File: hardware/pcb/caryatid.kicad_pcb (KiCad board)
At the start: 2 copper layers, 150 x 90 mm, 131 parts, among them J1 DC in, J10 FSR, J11 Digital bus, J12 RGB status, J13 Comms A - Qwiic, J14 Mic bias return, J15 Comms B - module, J16 Expansion / SPI1, J17 Audio out L/R/G, J18 Audio in L/R/rtn, J19 Comms A - module, J3 Latch switch, J4 Charge LEDs, J5 Analogue bus, J6 SW1 switch, J7 SW2 switch, J8 SW3 switch, J9 Soft pot, U1 BQ24074RGT, U2 TPS61023DRL, U3 74HC14, U4 MCP6002

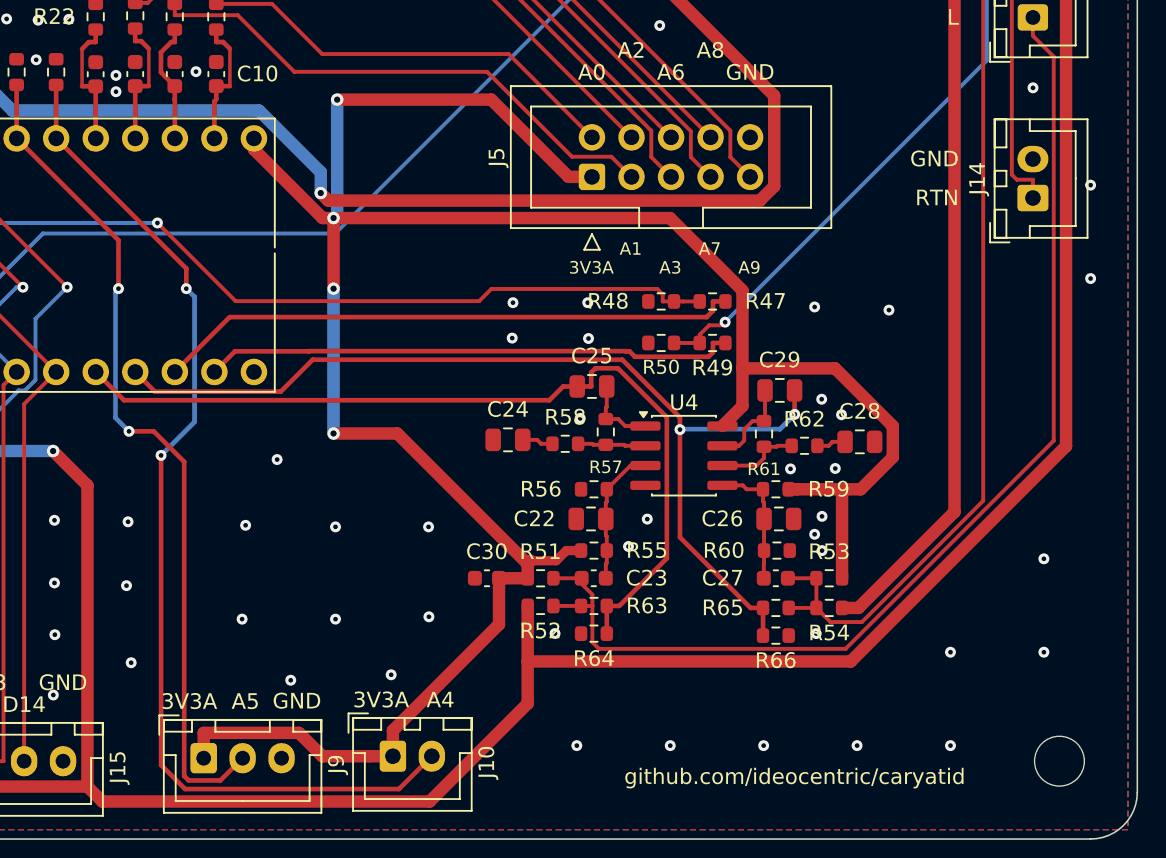
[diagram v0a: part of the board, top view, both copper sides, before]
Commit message: Source JP1-3: C52016391, verified against live JLC data
HX PH254-01-03-Z-L11.5, 1x3P 2.54mm through-hole header, 3A, gold
plated brass. 56393 in stock, MOQ 2, $0.0249 at 1-199, Extended,
manualWeld so JLC hand-solders it.

The L11.5 model number resolves to a 2.5 mm body with 6 mm of mating
pin, which is the length a standard 2.54 mm shunt needs, and puts the
top of a fitted shunt about 8.5 mm above the board -- far below the
26.91 mm stack, so it costs no headroom.

THE SHUNTS ARE NOT A PLACED COMPONENT. JLC will not fit a jumper cap;
it is an accessory, not a part on the board. Buying separately, noted
in lcsc.yaml so nobody looks for it on the BOM later.

Gate now reports 107 of 110 covered. The three still open are R51 2k2,
R52 220R and R67 392R -- and the first two were never a gap that got
missed: they were DNP, so they never reached a BOM export, and the
sourcing sweep only ever saw parts that do. Populating the front-end is
what surfaced them.

Recorded for the search: every 0603 resistor on this board is UNI-ROYAL
0603WAF series, all twelve of them, so the three outstanding values have
predictable manufacturer part numbers -- 0603WAF2201T5E, 0603WAF2200T5E
and 0603WAF3920T5E. The E24 values on this board are all Basic and the
E96 values all Extended, so R67 should be expected to carry a loading
fee and the other two not.
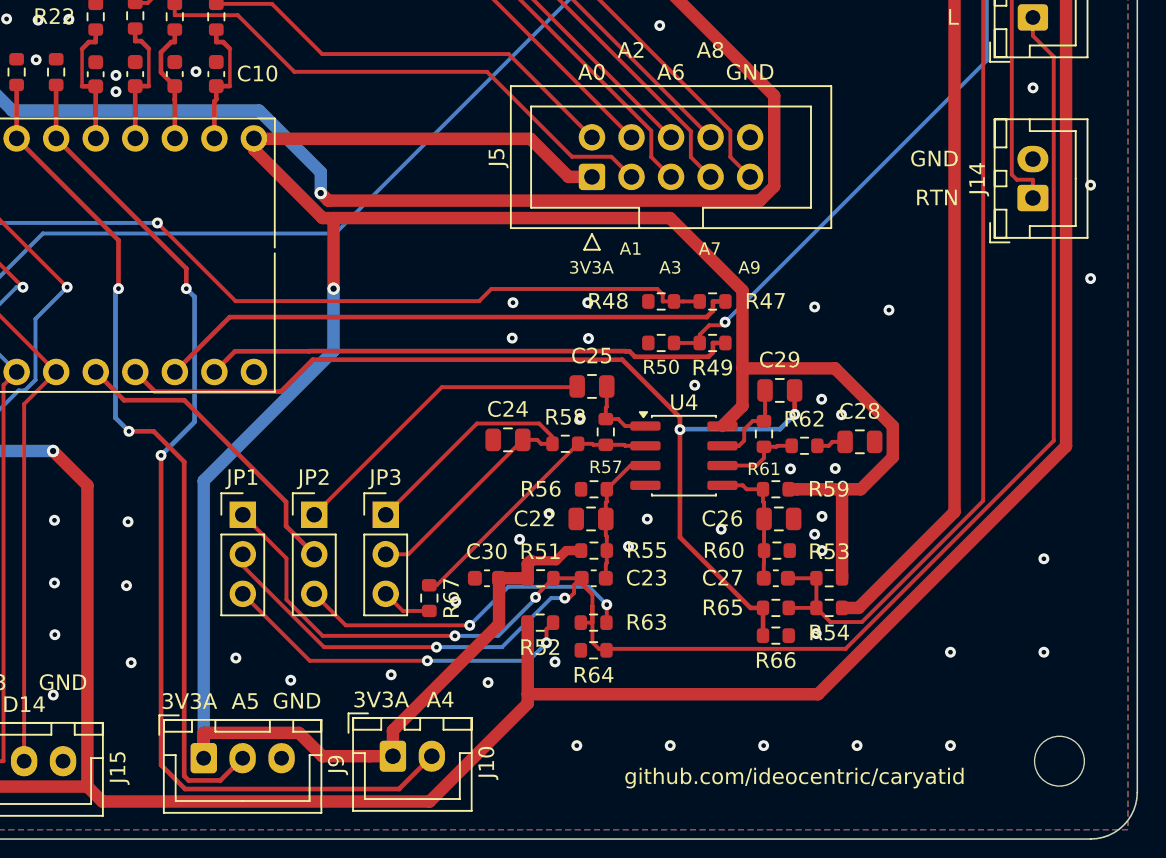
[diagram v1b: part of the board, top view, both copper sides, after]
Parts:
- added JP1: Mic bias select, Connector_PinHeader_2.54mm:PinHeader_1x03_P2.54mm_Vertical, F.Cu at (142.5, 99.2)
- added JP2: Mic path select, Connector_PinHeader_2.54mm:PinHeader_1x03_P2.54mm_Vertical, F.Cu at (147.1, 99.2)
- added JP3: Mic gain select, Connector_PinHeader_2.54mm:PinHeader_1x03_P2.54mm_Vertical, F.Cu at (151.7, 99.2)
- added R67: 392R, Resistor_SMD:R_0603_1608Metric, F.Cu at (154.5, 104.5)
- moved R52 1.07 mm to (161.7, 106.1)
- moved R63 1.07 mm to (165.1, 106.1)
- moved R64 1.07 mm to (165.1, 107.9)
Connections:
- C25 pad 2: AUDIO_IN_L -> AMP_OUT_L
- R51 pad 2: /audio/MIC_L -> /audio/BIAS_E_L
- R52 pad 2: /audio/MIC_L -> /audio/BIAS_C_L
- R58 pad 2: /audio/GAINLEG_L -> /audio/LEG_101_L
- R63 pad 2: AUDIO_IN_L -> BYPASS_L
- R64 pad 1: AUDIO_IN_L -> BYPASS_L
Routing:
- net AUDIO_IN_L: track 56.1 -> 19.8 mm
- net /audio/MIC_L: track 71.8 -> 97.9 mm, vias 0 -> 2
- net /audio/BIAS_E_L: track 0.00 -> 25.9 mm, vias 0 -> 2
- net /audio/BIAS_C_L: track 0.00 -> 23.2 mm, vias 0 -> 2
- net BYPASS_L: track 0.00 -> 22.3 mm, vias 0 -> 2
- net AMP_OUT_L: track 0.00 -> 20.3 mm
- net /audio/LEG_101_L: track 0.00 -> 13.5 mm
- net /audio/OPA_L_N: track 4.37 -> 17.7 mm
- net /audio/GAINLEG_L: track 2.01 -> 13.9 mm
- net +3V3A: track 162.6 -> 167.6 mm, vias 4 -> 1
- net /audio/LEG_256_L: track 0.00 -> 3.26 mm

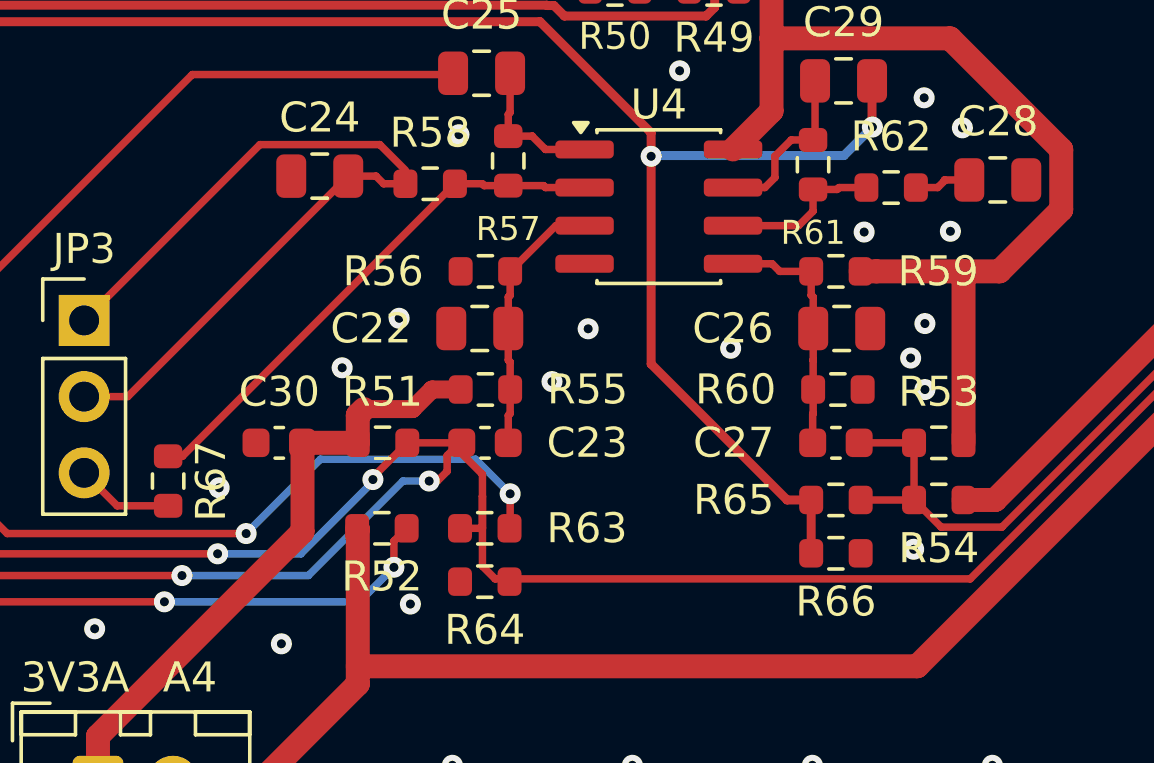
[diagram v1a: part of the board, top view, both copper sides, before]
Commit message: Delete four stale tracks the net split left shorting, and tidy up
Rewiring the mic front-end moved four pads onto new nets. KiCad reassigns
PAD nets on update but leaves existing TRACKS alone, so the tracks that
used to serve those pads stayed put and now touched pads of a different
net -- four real shorts that would have arrived as dead boards.

  GAINLEG_L  0.73 mm  shorting R58.2 LEG_101_L
  MIC_L      1.82 mm  shorting R51.2 BIAS_E_L
  MIC_L      0.60 mm  shorting R64.1 BYPASS_L
  MIC_L     15.84 mm  shorting R64.1 BYPASS_L

Matched on net AND both endpoints so no similar segment elsewhere could
be hit, and all four had to match or nothing was written.

A scan I wrote first reported 32 candidates and was wrong -- it treated
any track passing near a pad as overlapping, ignoring clearance. DRC is
the authority here and it says four. Recording that because the crude
version looked authoritative and would have sent someone chasing
twenty-eight phantoms.

Also: R67 reference moved from local -1.43 to -1.8 to clear the 0.25 mm
silk rule (it was 0.227 against its own outline), the 1x03 header height
recorded in check_board so the standoff check stops reporting unknowns,
and report-3.txt untracked and gitignored -- it was swept in by an
over-broad git add, along with the board work that landed in 3ed42ba
under a message about sourcing resistors. Nothing was lost; the message
simply did not describe the contents.

Remaining, and all needing KiCad: three MIC_L stubs now dangling,
R63.2 to R64.1 unrouted, and the GND planes wanting a refill.
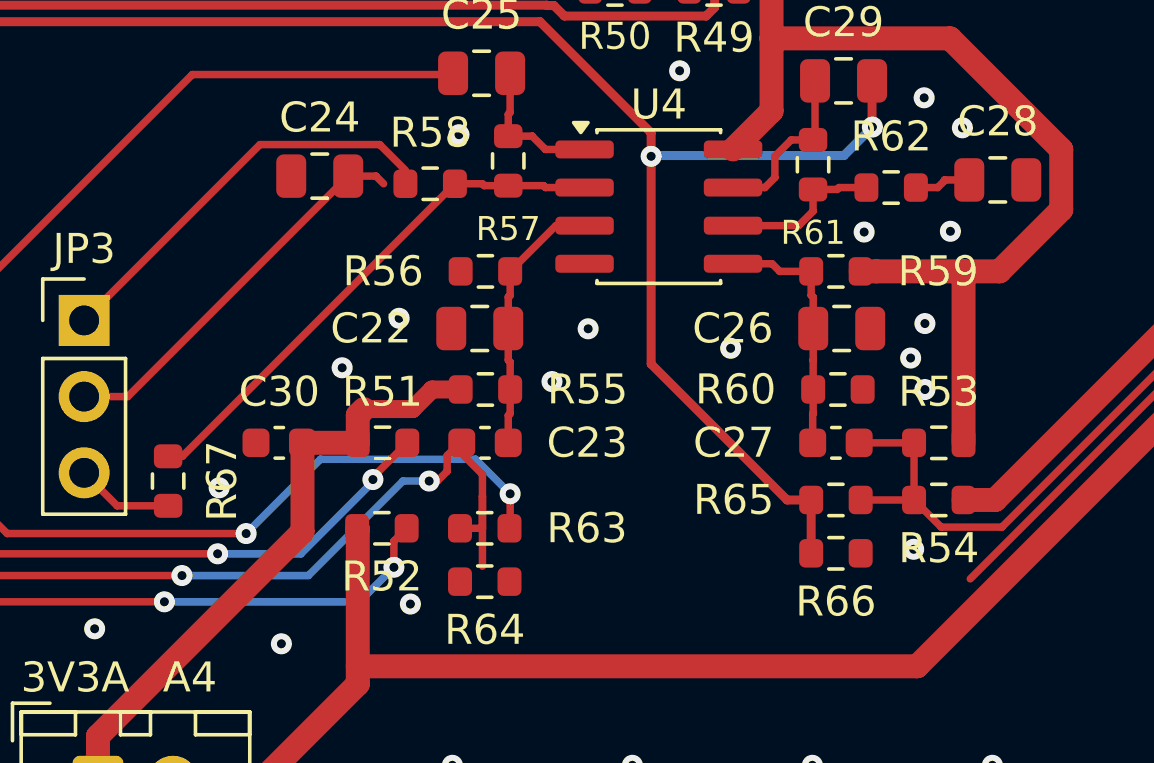
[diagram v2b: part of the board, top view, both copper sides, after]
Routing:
- net /audio/MIC_L: track 97.9 -> 79.7 mm
- net /audio/GAINLEG_L: track 13.9 -> 13.1 mm
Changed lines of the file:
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@@
 		(tags "resistor")
 		(property "Reference" "R67"
-			(at 0 -1.43 90)
+			(at 0 -1.8 90)
 			(layer "F.SilkS")
 			(effects
@@
 	)
 	(segment
-		(start 162.434 94.615)
-		(end 161.7073 94.615)
-		(width 0.25)
-		(layer "F.Cu")
-		(net 5)
-	)
-	(segment
 		(start 160.528 94.361)
 		(end 161.4533 94.361)
@@
 	)
 	(segment
-		(start 165.4242 107.7857)
-		(end 165.0017 107.3632)
-		(width 0.25)
-		(layer "F.Cu")
-		(net 7)
-	)
-	(segment
 		(start 165.0017 104.3017)
 		(end 165.0017 105.029)
@@
 	)
 	(segment
-		(start 181.261 107.7857)
-		(end 165.4242 107.7857)
-		(width 0.25)
-		(layer "F.Cu")
-		(net 7)
-	)
-	(segment
 		(start 194.6328 69.7455)
 		(end 194.6328 94.4139)
@@
 		(width 0.25)
 		(layer "F.Cu")
-		(net 7)
-	)
-	(segment
-		(start 164.312 103.251)
-		(end 162.496 103.251)
-		(width 0.25)
-		(layer "F.Cu")

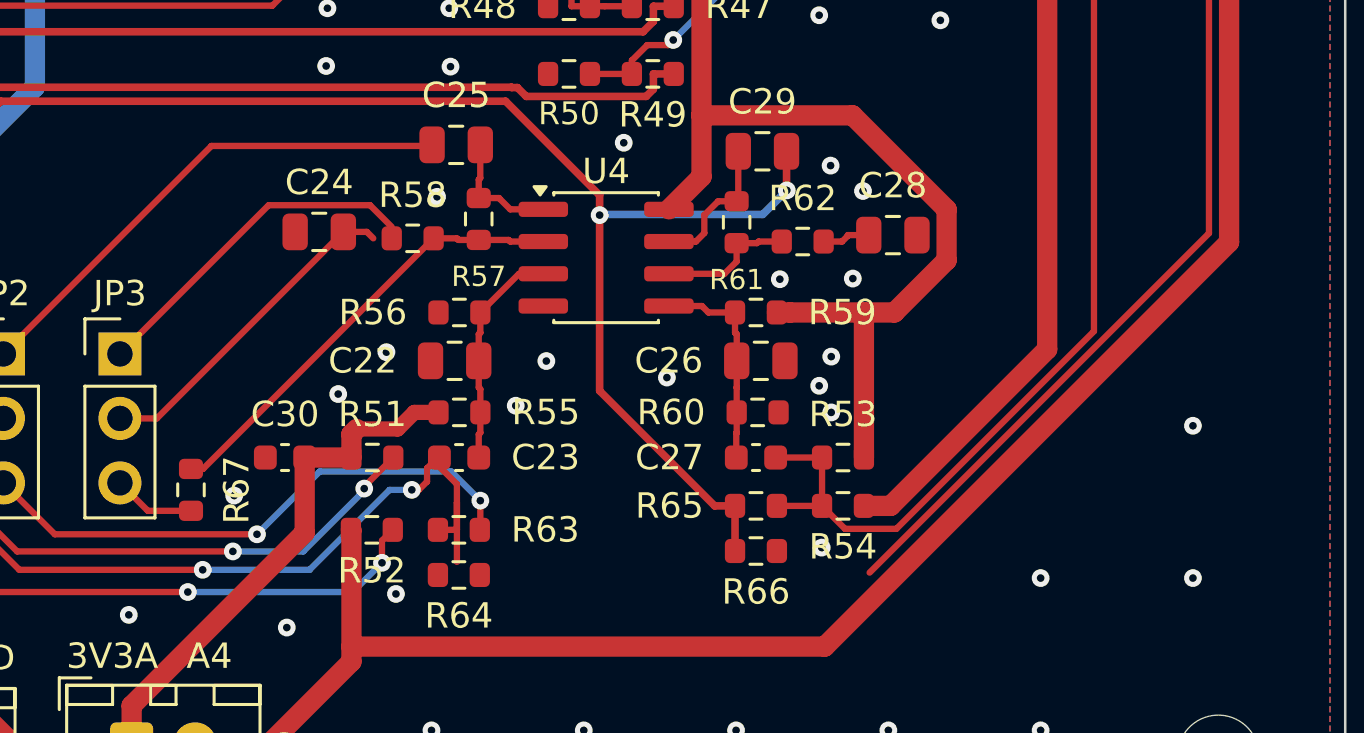
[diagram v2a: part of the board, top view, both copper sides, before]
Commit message: Add check 11: orphaned ground pour, and fix the cost tool BOM columns
The mic jumper routing fenced off a 17.7 mm2 island of F.Cu ground pour
directly under the analogue front end -- copper at floating potential
sitting beside signal traces, which couples instead of shielding.

NOTHING POINTED AT IT. All ten checks here passed. KiCad DRC caught it
only as "Zone GND on F.Cu / on B.Cu unconnected", reported at the zone
ORIGIN in the opposite corner of the board, tens of millimetres from the
actual island. The report told you something was wrong and nothing about
where.

Check 11 tests every filled GND region for a via or through-hole pad
inside it and names the area and bounding box when it finds none. Slivers
under 0.5 mm2 are ignored as fill artefacts.

Verified by reproduction, not by assertion: deleting the via that
rescued the island makes the check report exactly 17.7 mm2 at
X 151.8-159.7 Y 93.7-101.3, and restoring it passes.

Also fixed cost_estimate.py, which was reading "LCSC" and "QUANTITY"
columns that no longer exist -- the BOM moved to JLC template columns
(Comment / Designator / Footprint / JLCPCB Part #) with no quantity
field, so the count is now the number of designators. It had been broken
since that change and nothing exercised it until now.
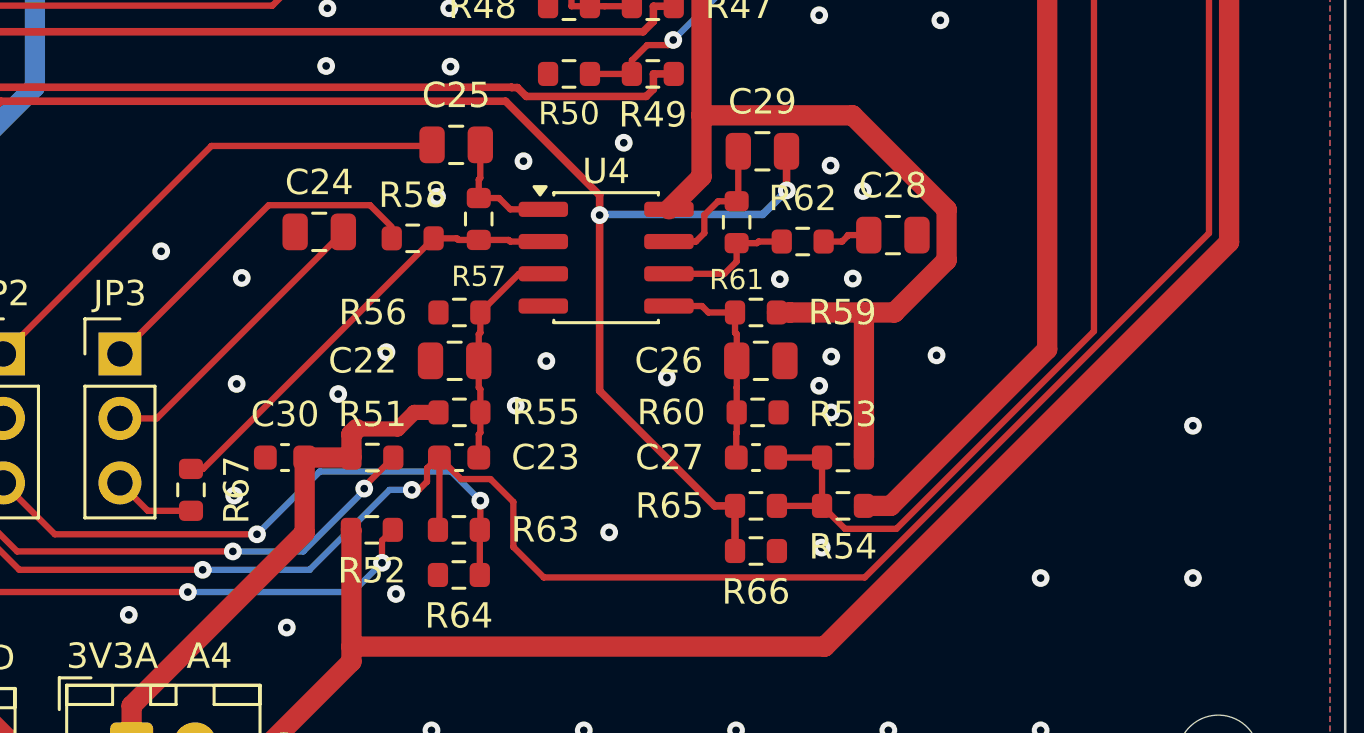
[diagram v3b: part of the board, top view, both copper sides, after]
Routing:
- net /audio/MIC_L: track 79.7 -> 96.4 mm
- net BYPASS_L: track 22.3 -> 24.1 mm
- net /audio/GAINLEG_L: track 13.1 -> 11.8 mm
- net GND: vias 145 -> 151
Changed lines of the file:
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@@
 	)
 	(segment
-		(start 160.528 94.361)
-		(end 161.4533 94.361)
-		(width 0.25)
-		(layer "F.Cu")
-		(net 5)
-	)
-	(segment
-		(start 161.4533 94.361)
-		(end 161.7073 94.615)
-		(width 0.25)
-		(layer "F.Cu")
-		(net 5)
-	)
-	(segment
 		(start 179.45 94.742)
 		(end 180.1767 94.742)
@@
 	)
 	(segment
-		(start 165.0017 107.3632)
-		(end 165.0017 105.029)
+		(start 181.0717 107.975)
+		(end 168.425 107.975)
 		(width 0.25)
 		(layer "F.Cu")
@@
 	)
 	(segment
-		(start 165.0017 104.3017)
-		(end 165.0017 105.029)
+		(start 163.825 103.675)
+		(end 164.249 103.251)
 		(width 0.25)
 		(layer "F.Cu")
@@
 	)
 	(segment
-		(start 163.825 103.675)
-		(end 164.249 103.251)
+		(start 168.425 107.975)
+		(end 167.225 106.775)
 		(width 0.25)
 		(layer "F.Cu")
@@
 	)
 	(segment
-		(start 193.294 67.23)
-		(end 193.294 68.4067)
+		(start 194.6328 94.4139)
+		(end 181.0717 107.975)
 		(width 0.25)
 		(layer "F.Cu")
@@
 	)
 	(segment
-		(start 164.312 103.612)
-		(end 165.0017 104.3017)
+		(start 164.3 106.1)
+		(end 164.254 106.1)
 		(width 0.25)
 		(layer "F.Cu")
@@
 	)
 	(segment
-		(start 164.312 103.251)
-		(end 164.312 103.612)
+		(start 164.249 103.251)
+		(end 164.312 103.251)
 		(width 0.25)
 		(layer "F.Cu")
@@
 	)
 	(segment
-		(start 164.249 103.251)
+		(start 165.161 104.1)
 		(end 164.312 103.251)
 		(width 0.25)
@@
 	)
 	(segment
-		(start 165.0017 106.1)
+		(start 164.312 106.042)
 		(end 164.254 106.1)
 		(width 0.25)
@@
 	)
 	(segment
-		(start 165.0017 105.029)
-		(end 165.0017 106.1)
+		(start 167.225 106.775)
+		(end 167.225 105)
 		(width 0.25)
 		(layer "F.Cu")
@@
 	)
 	(segment
-		(start 163.5 104.525)
-		(end 163.825 104.2)
+		(start 193.294 68.4067)
+		(end 194.6328 69.7455)
 		(width 0.25)
 		(layer "F.Cu")
@@
 	)
 	(segment
-		(start 193.294 68.4067)
-		(end 194.6328 69.7455)
+		(start 164.312 103.251)
+		(end 164.312 106.042)
+		(width 0.25)
+		(layer "F.Cu")
+		(net 7)
+	)
+	(segment
+		(start 194.6328 69.7455)
+		(end 194.6328 94.4139)
+		(width 0.25)
+		(layer "F.Cu")
+		(net 7)
+	)
+	(segment
+		(start 193.294 67.23)
+		(end 193.294 68.4067)
+		(width 0.25)
+		(layer "F.Cu")
+		(net 7)
+	)
+	(segment
+		(start 166.325 104.1)
+		(end 165.161 104.1)
+		(width 0.25)
+		(layer "F.Cu")
+		(net 7)
+	)
+	(segment
+		(start 163.5 104.525)
+		(end 163.825 104.2)
 		(width 0.25)
 		(layer "F.Cu")
@@
 	)
 	(segment
-		(start 194.6328 69.7455)
-		(end 194.6328 94.4139)
+		(start 167.225 105)
+		(end 166.325 104.1)
 		(width 0.25)
 		(layer "F.Cu")
@@
 		(net 7)
 	)
-	(segment
-		(start 194.6328 94.4139)
-		(end 181.261 107.7857)
-		(width 0.25)
-		(layer "F.Cu")
-		(net 7)
-	)
 	(via
 		(at 163.225 104.525)
@@
 	)
 	(via
+		(at 183.9 99.225)
+		(size 0.7)
+		(drill 0.3)
+		(layers "F.Cu" "B.Cu")
+		(free yes)
+		(net 91)
+	)
+	(via
 		(at 164.22 92.98)
 		(size 0.7)
@@
 	)
 	(via
+		(at 156.525 96.175)
+		(size 0.7)
+		(drill 0.3)
+		(layers "F.Cu" "B.Cu")
+		(free yes)
+		(net 91)
+	)
+	(via
 		(at 88.9 110.2)
 		(size 0.7)
@@
 	)
 	(via
+		(at 153.35 95.125)
+		(size 0.7)
+		(drill 0.3)
+		(layers "F.Cu" "B.Cu")
+		(free yes)
+		(net 91)
+	)
+	(via
 		(at 124.225 67.525)
 		(size 0.7)
@@
 	)
 	(via
+		(at 167.625 91.575)
+		(size 0.7)
+		(drill 0.3)
+		(layers "F.Cu" "B.Cu")
+		(free yes)
+		(net 91)
+	)
+	(via
 		(at 179.275 85.825)
 		(size 0.7)
@@
 	)
 	(via
+		(at 171 106.2)
+		(size 0.7)
+		(drill 0.3)
+		(layers "F.Cu" "B.Cu")
+		(free yes)
+		(net 91)
+	)
+	(via
 		(at 179.725 91.75)
 		(size 0.7)
@@
 	)
 	(via
+		(at 156.325 100.35)
+		(size 0.7)
+		(drill 0.3)
+		(layers "F.Cu" "B.Cu")
+		(free yes)
+		(net 91)
+	)
+	(via
 		(at 179.75 101.475)
 		(size 0.7)
@@
 		(width 0.25)
 		(layer "F.Cu")
+		(net 105)
+	)
+	(segment
+		(start 165.904 106.1)
+		(end 165.904 107.878)
+		(width 0.25)
+		(layer "F.Cu")
